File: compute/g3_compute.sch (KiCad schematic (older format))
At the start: 15 parts, among them J101 CONSMA001-SMD-G, J102 Temp_Connector_1x4, U101 PA1616D, U102 LoRa-E5

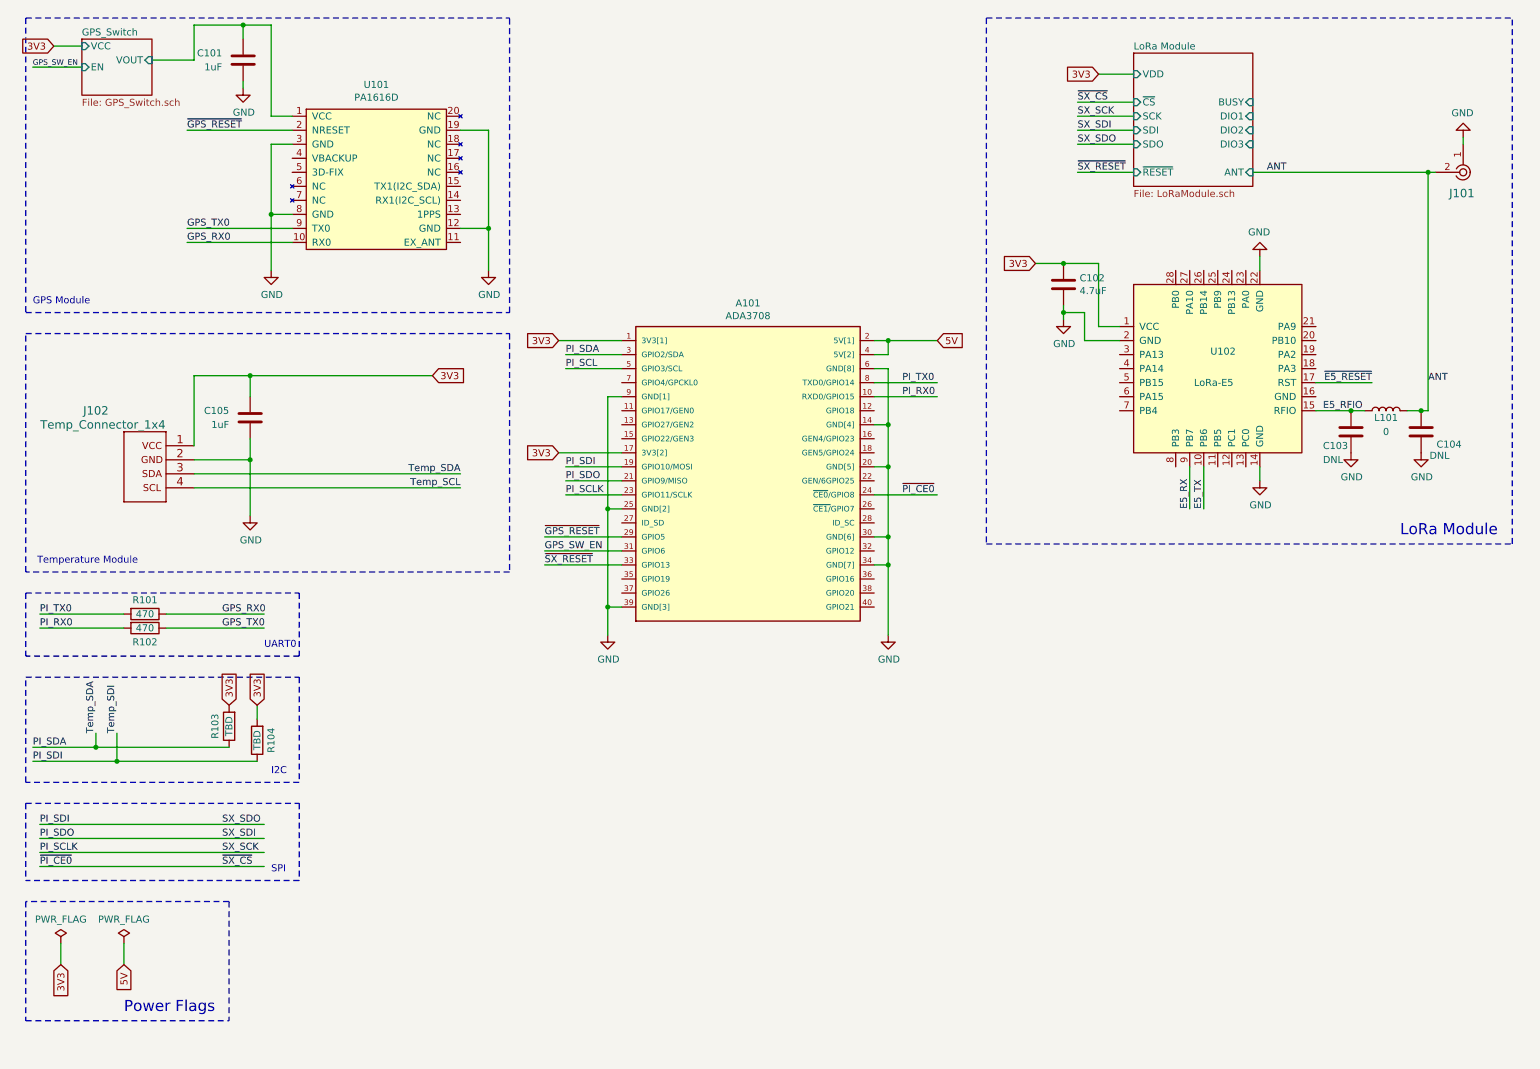
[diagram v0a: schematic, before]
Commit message: updated compute schematic with test points and UART connections
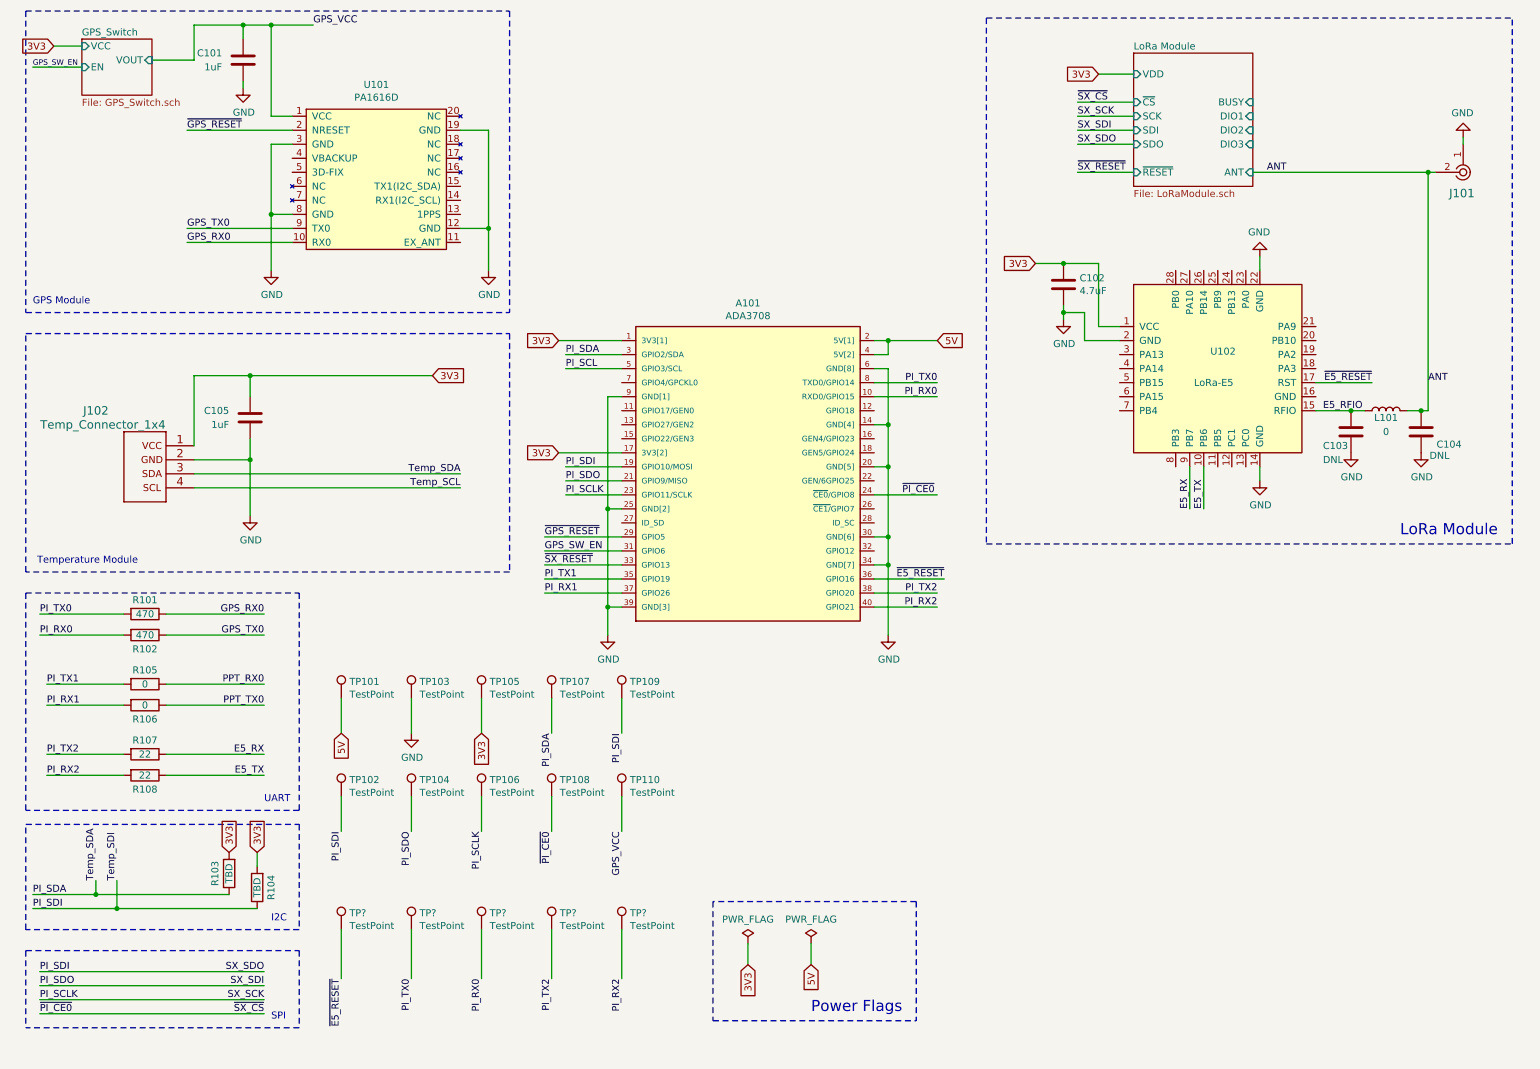
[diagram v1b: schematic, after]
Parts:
- added R105, R106: 0, Resistor_SMD:R_0402_1005Metric_Pad0.72x0.64mm_HandSolder, symbol Device:R
- added R107, R108: 22, Resistor_SMD:R_0402_1005Metric_Pad0.72x0.64mm_HandSolder, symbol Device:R
- added TP101, TP102, TP103, TP104, TP105, TP106, TP107, TP108, TP109, TP110, TP? (x5): TestPoint, symbol Connector:TestPoint
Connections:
- net labels added: GPS_VCC, PI_RX1, PI_RX2, PI_TX1, PI_TX2, PPT_RX0, PPT_TX0
- wire segments 108 -> 137
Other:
- note added: "UART"
- note removed: "UART0"
- moved on the sheet: R102, R103, R104

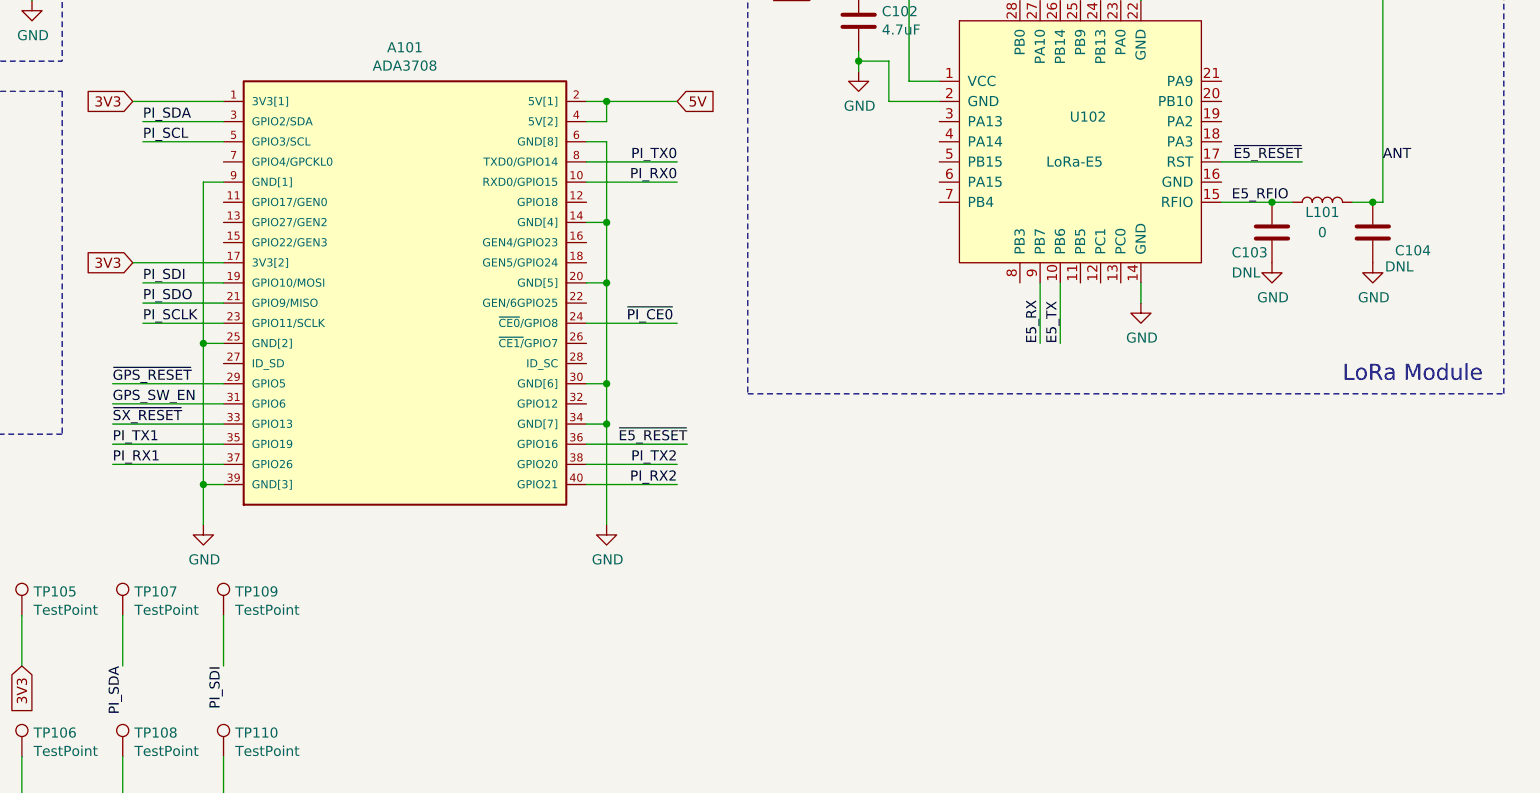
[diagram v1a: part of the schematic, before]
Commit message: added remaining GPIO on PI to a header
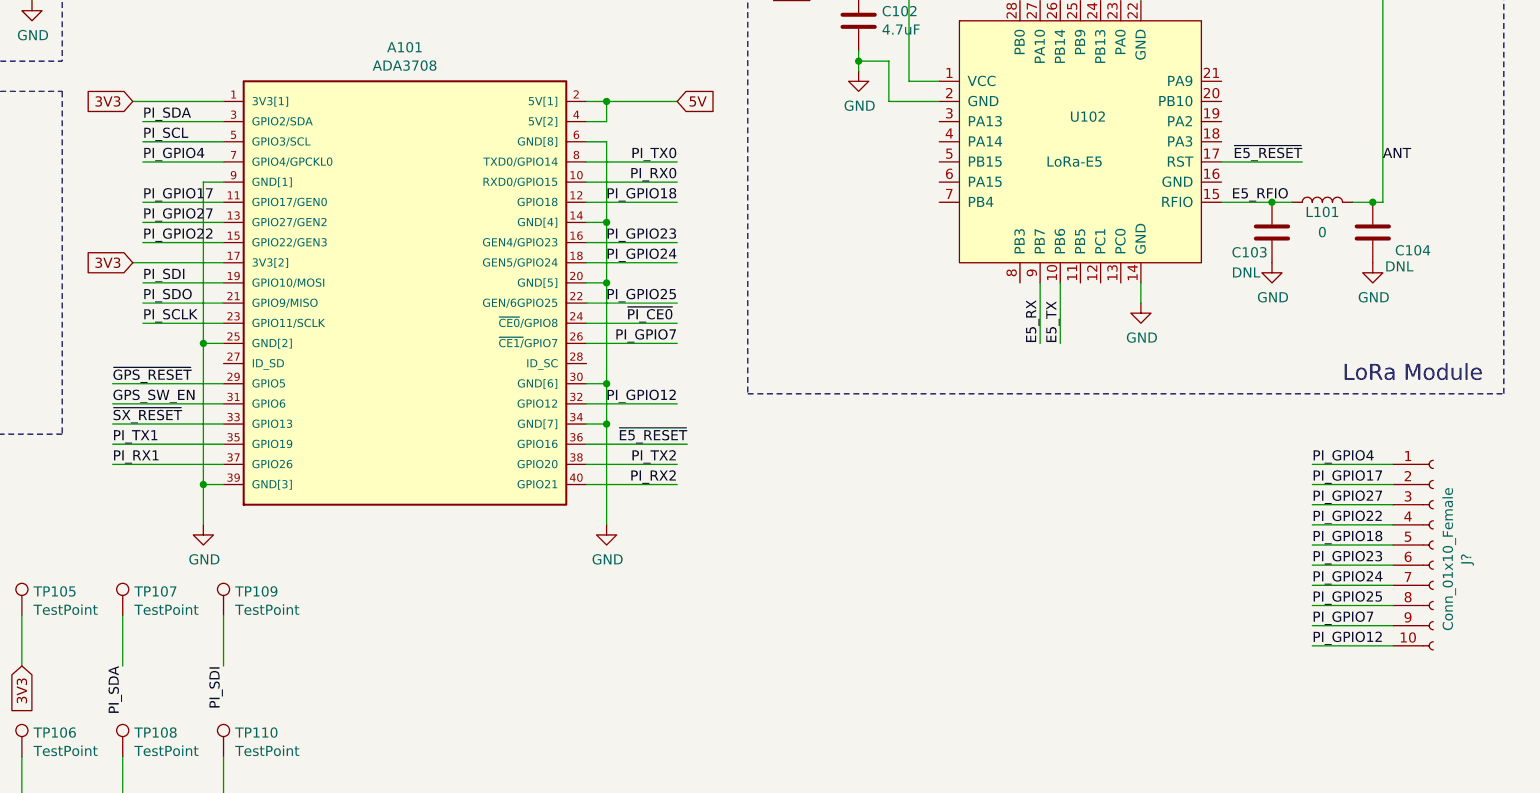
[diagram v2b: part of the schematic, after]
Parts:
- added J?: Conn_01x10_Female, symbol Connector:Conn_01x10_Female
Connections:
- net PI_GPIO17: now reaches A101.11 (GPIO17/GEN0)
- net PI_GPIO17: now also J?.2 (Pin_2)
- net PI_GPIO18: now reaches A101.12 (GPIO18)
- net PI_GPIO18: now also J?.5 (Pin_5)
- net PI_GPIO27: now reaches A101.13 (GPIO27/GEN2)
- net PI_GPIO27: now also J?.3 (Pin_3)
- net PI_GPIO22: now reaches A101.15 (GPIO22/GEN3)
- net PI_GPIO22: now also J?.4 (Pin_4)
- net PI_GPIO23: now reaches A101.16 (GEN4/GPIO23)
- net PI_GPIO23: now also J?.6 (Pin_6)
- net PI_GPIO24: now reaches A101.18 (GEN5/GPIO24)
- net PI_GPIO24: now also J?.7 (Pin_7)
- net PI_GPIO25: now reaches A101.22 (GEN/6GPIO25)
- net PI_GPIO25: now also J?.8 (Pin_8)
- net PI_GPIO7: now reaches A101.26 (~CE1/~GPIO7)
- net PI_GPIO7: now also J?.9 (Pin_9)
- net PI_GPIO12: now reaches A101.32 (GPIO12)
- net PI_GPIO12: now also J?.10 (Pin_10)
- net PI_GPIO4: now reaches A101.7 (GPIO4/GPCKL0)
- net PI_GPIO4: now also J?.1 (Pin_1)
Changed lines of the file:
@@
 Text Label 4800 7400 3    50   ~ 0
 PI_RX2
+Wire Wire Line
+	4800 3550 4400 3550
+Wire Wire Line
+	4800 3450 4400 3450
+Wire Wire Line
+	4800 3350 4400 3350
+Wire Wire Line
+	4800 3150 4400 3150
+Wire Wire Line
+	6600 3350 7050 3350
+Wire Wire Line
+	6600 3550 7050 3550
+Wire Wire Line
+	6600 3650 7050 3650
+Wire Wire Line
+	6600 3850 7050 3850
+Wire Wire Line
+	6600 4050 7050 4050
+Wire Wire Line
+	6600 4350 7050 4350
+Text Label 4400 3150 0    50   ~ 0
+PI_GPIO4
+Text Label 4400 3350 0    50   ~ 0
+PI_GPIO17
+Text Label 4400 3450 0    50   ~ 0
+PI_GPIO27
+Text Label 4400 3550 0    50   ~ 0
+PI_GPIO22
+Text Label 7050 3350 2    50   ~ 0
+PI_GPIO18
+Text Label 7050 3550 2    50   ~ 0
+PI_GPIO23
+Text Label 7050 3650 2    50   ~ 0
+PI_GPIO24
+Text Label 7050 3850 2    50   ~ 0
+PI_GPIO25
+Text Label 7050 4050 2    50   ~ 0
+PI_GPIO7
+Text Label 7050 4350 2    50   ~ 0
+PI_GPIO12
+$Comp
+L Connector:Conn_01x10_Female J?
+U 1 1 61DEF596
+P 10800 5050
+F 0 "J?" V 10965 4980 50  0000 C CNN
+F 1 "Conn_01x10_Female" V 10874 4980 50  0000 C CNN
+F 2 "" H 10800 5050 50  0001 C CNN
+F 3 "~" H 10800 5050 50  0001 C CNN
+	1    10800 5050
+	1    0    0    -1
+$EndComp
+Wire Wire Line
+	10600 4650 10200 4650
+Wire Wire Line
+	10600 4750 10200 4750
+Wire Wire Line
+	10200 4850 10600 4850
+Wire Wire Line
+	10600 4950 10200 4950
+Wire Wire Line
+	10600 5050 10200 5050
+Wire Wire Line
+	10600 5150 10200 5150
+Wire Wire Line
+	10600 5250 10200 5250
+Wire Wire Line
+	10600 5350 10200 5350
+Wire Wire Line
+	10600 5450 10200 5450
+Wire Wire Line
+	10600 5550 10200 5550
+Text Label 10200 4650 0    50   ~ 0
+PI_GPIO4
+Text Label 10200 4750 0    50   ~ 0
+PI_GPIO17
+Text Label 10200 4850 0    50   ~ 0
+PI_GPIO27
+Text Label 10200 4950 0    50   ~ 0
+PI_GPIO22
+Text Label 10200 5050 0    50   ~ 0
+PI_GPIO18
+Text Label 10200 5150 0    50   ~ 0
+PI_GPIO23
+Text Label 10200 5250 0    50   ~ 0
+PI_GPIO24
+Text Label 10200 5350 0    50   ~ 0
+PI_GPIO25
+Text Label 10200 5450 0    50   ~ 0
+PI_GPIO7
+Text Label 10200 5550 0    50   ~ 0
+PI_GPIO12
 $EndSCHEMATC

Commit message: rework on sch and layout
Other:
- note added: "Test Points"
- moved on the sheet: A101, J?, TP101, TP102, TP103, TP104, TP105, TP106, TP107, TP108, TP109, TP110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

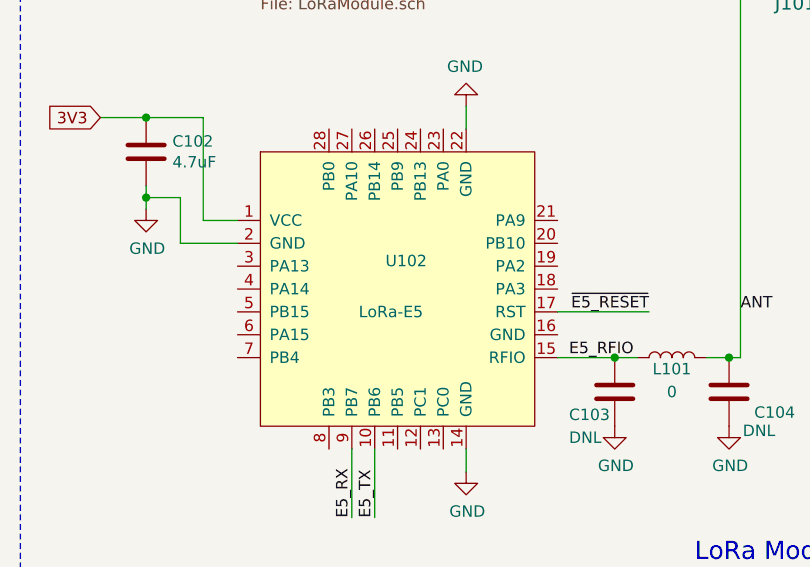
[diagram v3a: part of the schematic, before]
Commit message: BOM fields changes to LoRa module
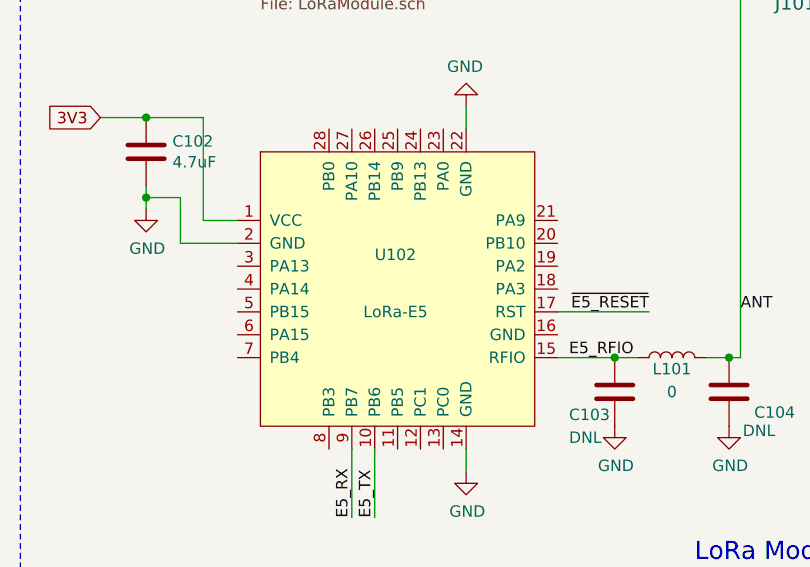
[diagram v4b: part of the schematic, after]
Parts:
- J101: Category Connectors, Interconnects -> (none); DK_Datasheet_Link https://linxtechnologies.com/wp/wp-content/uploads/consma00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 -> (none); DK_Detail_Page /product-detail/en/linx-technologies-inc/CONSMA001-SMD-G/CO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 -> (none); Description CONN SMA RCPT STR 50 OHM SMD -> (none); Digi-Key_PN CONSMA001-SMD-G-ND -> (none); Family Coaxial Connectors (RF) -> (none); MFN (none) -> Linx Technologies Inc.; MFP (none) -> CONSMA001-SMD-G; MPN CONSMA001-SMD-G -> (none); Manufacturer Linx Technologies Inc. -> (none); S1PL (none) -> /product-detail/en/linx-technologies-inc/CONSMA001-SMD-G/CO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; S1PN (none) -> CONSMA001-SMD-G-ND; Status Active -> (none)
- U102: Description LoRa Module -> (none); MFN (none) -> SeeedStudio; MFP (none) -> LoRa-E5; S1PL (none) -> https://www.seeedstudio.com/LoRa-E5-Wireless-Module-p-4745.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; S1PN (none) -> LoRa-E5
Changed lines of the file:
@@
 	2100 600  2100 700
-$Comp
-L Transceivers:LoRa-E5 U102
-U 1 1 6195631D
-P 9050 3050
-F 0 "U102" H 8997 3173 50  0000 L CNN
-F 1 "LoRa-E5" H 8880 2950 50  0000 L CNN
-F 2 "Perch:LoRa-E5" H 9700 2400 50  0001 C CNN
-F 3 "https://files.seeedstudio.com/products/317990687/res/LoRa-E5%20module%20datasheet_V1.0.pdf" H 9050 3050 50  0001 C CNN
-F 4 "LoRa Module" H 9050 3050 50  0001 C CNN "Description"
-	1    9050 3050
-	1    0    0    -1
-$EndComp
 $Comp
 L power:PWR_FLAG #FLG0101
@@
 F 9 "https://www.mouser.com/ProductDetail/YAGEO/CC0402KRX5R5BB475?qs=UgE/0m3bTsY3XUxTV5ZyKA==&utm_source=netcomponents&utm_medium=aggregator&utm_campaign=CC0402KRX5R5BB475&utm_content=YAGEO" H 7950 2450 50  0001 C CNN "S2PL"
 F 10 "603-CC0402KRX55BB475" H 7950 2450 50  0001 C CNN "S2PN"
+F 11 "" H 7950 2450 50  0001 C CNN "Notes"
 	1    7950 2450
 	1    0    0    -1
@@
 F 2 "digikey-footprints:RF_SMA_Receptical_Vertical_CONSMA001-SMD-G" H 11000 1850 60  0001 L CNN
 F 3 "https://linxtechnologies.com/wp/wp-content/uploads/consma001-smd-g.pdf" H 11000 1950 60  0001 L CNN
-F 4 "CONSMA001-SMD-G-ND" H 11000 2050 60  0001 L CNN "Digi-Key_PN"
-F 5 "CONSMA001-SMD-G" H 11000 2150 60  0001 L CNN "MPN"
-F 6 "Connectors, Interconnects" H 11000 2250 60  0001 L CNN "Category"
-F 7 "Coaxial Connectors (RF)" H 11000 2350 60  0001 L CNN "Family"
-F 8 "https://linxtechnologies.com/wp/wp-content/uploads/consma001-smd-g.pdf" H 11000 2450 60  0001 L CNN "DK_Datasheet_Link"
-F 9 "/product-detail/en/linx-technologies-inc/CONSMA001-SMD-G/CONSMA001-SMD-G-ND/4496569" H 11000 2550 60  0001 L CNN "DK_Detail_Page"
-F 10 "CONN SMA RCPT STR 50 OHM SMD" H 11000 2650 60  0001 L CNN "Description"
-F 11 "Linx Technologies Inc." H 11000 2750 60  0001 L CNN "Manufacturer"
-F 12 "Active" H 11000 2850 60  0001 L CNN "Status"
+F 4 "Linx Technologies Inc." H 11000 2750 60  0001 L CNN "MFN"
+F 5 "CONSMA001-SMD-G" H 11000 2150 60  0001 L CNN "MFP"
+F 6 "CONSMA001-SMD-G-ND" H 11000 2050 60  0001 L CNN "S1PN"
+F 7 "/product-detail/en/linx-technologies-inc/CONSMA001-SMD-G/CONSMA001-SMD-G-ND/4496569" H 11000 2550 60  0001 L CNN "S1PL"
+F 8 "" H 10800 1650 50  0001 C CNN "Notes"
 	1    10800 1650
 	-1   0    0    1
@@
 F 2 "Inductor_SMD:L_0402_1005Metric_Pad0.77x0.64mm_HandSolder" H 10250 3350 50  0001 C CNN
 F 3 "~" H 10250 3350 50  0001 C CNN
+F 4 "" V 10250 3350 50  0001 C CNN "MFN"
+F 5 "" V 10250 3350 50  0001 C CNN "MFP"
+F 6 "" V 10250 3350 50  0001 C CNN "S1PN"
+F 7 "" V 10250 3350 50  0001 C CNN "S1PL"
+F 8 "" V 10250 3350 50  0001 C CNN "Notes"
 	1    10250 3350
 	0    -1   -1   0
@@
 F 2 "Capacitor_SMD:C_0402_1005Metric_Pad0.74x0.62mm_HandSolder" H 10038 3350 50  0001 C CNN
 F 3 "~" H 10000 3500 50  0001 C CNN
+F 4 "" H 10000 3500 50  0001 C CNN "MFN"
+F 5 "" H 10000 3500 50  0001 C CNN "MFP"
+F 6 "" H 10000 3500 50  0001 C CNN "S1PN"
+F 7 "" H 10000 3500 50  0001 C CNN "S1PL"
+F 8 "" H 10000 3500 50  0001 C CNN "Notes"
 	1    10000 3500
 	1    0    0    -1
@@
 F 2 "Capacitor_SMD:C_0402_1005Metric_Pad0.74x0.62mm_HandSolder" H 10538 3350 50  0001 C CNN
 F 3 "~" H 10500 3500 50  0001 C CNN
+F 4 "" H 10500 3500 50  0001 C CNN "MFN"
+F 5 "" H 10500 3500 50  0001 C CNN "MFP"
+F 6 "" H 10500 3500 50  0001 C CNN "S1PN"
+F 7 "" H 10500 3500 50  0001 C CNN "S1PL"
+F 8 "" H 10500 3500 50  0001 C CNN "Notes"
 	1    10500 3500
 	1    0    0    -1
@@
 Text Notes 5950 7650 0    50   ~ 0
 Test Points
+$Comp
+L Transceivers:LoRa-E5 U102
+U 1 1 61C457FB
+P 9050 3050
+F 0 "U102" H 8950 3200 50  0000 L CNN
+F 1 "LoRa-E5" H 8900 2950 50  0000 L CNN
+F 2 "Perch:LoRa-E5" H 8750 2000 50  0001 C CNN
+F 3 "https://files.seeedstudio.com/products/317990687/res/LoRa-E5%20module%20datasheet_V1.0.pdf" H 9050 3050 50  0001 C CNN
+F 4 "SeeedStudio" H 8700 1900 50  0001 C CNN "MFN"
+F 5 "LoRa-E5" H 8650 1700 50  0001 C CNN "MFP"
+F 6 "LoRa-E5" H 8700 1800 50  0001 C CNN "S1PN"
+F 7 "https://www.seeedstudio.com/LoRa-E5-Wireless-Module-p-4745.html" H 9850 1600 50  0001 C CNN "S1PL"
+	1    9050 3050
+	1    0    0    -1
+$EndComp
 $EndSCHEMATC
